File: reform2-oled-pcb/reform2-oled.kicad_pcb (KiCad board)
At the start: 2 copper layers, 80 x 12 mm, 14 parts, among them J1 AUX, U1 SSD1306

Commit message: WIP OLED now CERN-OHL-S 2.0
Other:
- board text added: "REFORM OLED 2.0D-4 2020-04-12 MNTRE.COM LICENSE: CERN-OHL-S 2.0"
- board text removed: "REFORM OLED 2.0D-3 2020-03-05 MNTRE.COM"
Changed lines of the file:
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@@
-(kicad_pcb (version 20171130) (host pcbnew 5.1.2+dfsg1-1)
+(kicad_pcb (version 20171130) (host pcbnew 5.1.5+dfsg1-2+b1)
   (general
     (thickness 1.6)
@@
     (arrow2b (pts (xy 180.4 86.5) (xy 179.273496 87.086421)))
   )
-  (gr_text "REFORM OLED 2.0D-3\n2020-03-05 MNTRE.COM\n" (at 109.6 91.5) (layer B.SilkS)
+  (gr_text "REFORM OLED 2.0D-4\n2020-04-12 MNTRE.COM\nLICENSE: CERN-OHL-S 2.0" (at 104.4 97.2) (layer B.SilkS)
     (effects (font (size 1 1) (thickness 0.15) italic) (justify right mirror))
   )

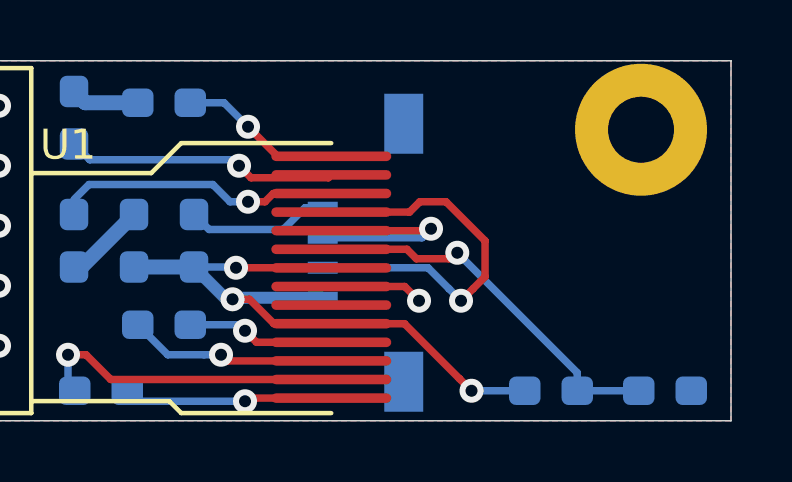
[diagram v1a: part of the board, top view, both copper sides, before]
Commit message: reform2-oled: fix: swap sda/scl
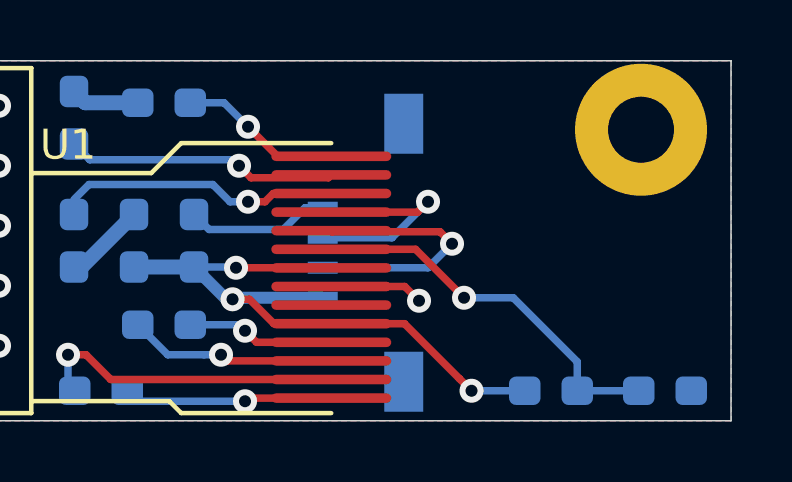
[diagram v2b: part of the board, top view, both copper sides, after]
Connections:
- J1 pad 2: DISP_SCL -> DISP_SDA
- J1 pad 3: DISP_SDA -> DISP_SCL
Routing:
- net DISP_SDA: track 13.2 -> 7.37 mm
- net DISP_SCL: track 7.09 -> 8.85 mm
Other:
- board text added: "REFORM OLED 2.0D-4 2020-04-19 MNTRE.COM LICENSE: CERN-OHL-S 2.0"
- board text removed: "REFORM OLED 2.0D-4 2020-04-12 MNTRE.COM LICENSE: CERN-OHL-S 2.0"
